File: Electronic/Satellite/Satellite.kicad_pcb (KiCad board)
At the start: 4 copper layers, 50 x 50 mm, 134 parts, among them CN1 SM04B-SRSS-TB, CN2 SM04B-SRSS-TB, J1 Conn02_Pin, J2 Conn02_Pin, J3 Conn02_Pin, J4 Conn02_Pin, J5 TC2050, J6 Conn_01x12_Pin, J7 Conn_01x12_Pin, SW1 TS-1088-AR02016, SW2 TS-1088-AR02016, U1 LAN8651B1-E/LMX, U10 SRR1280-560M, U11 NCP1117ST33T3G, U12 RP2354A, U13 WS2812C-2020-V6, U2 AVRH10C221KT1R5YA8, U3 MCP2518FDT-E/SL, U4 ATA6563-GAQW1, U5 AVRH10C221KT1R5YA8, U6 SY8513FCC, U7 MAX3232IPWR, U8 AL8860QMP-13, U9 ABM8-272-T3_C20625731, X1 ABM10-25.000MHZ-D30-T3

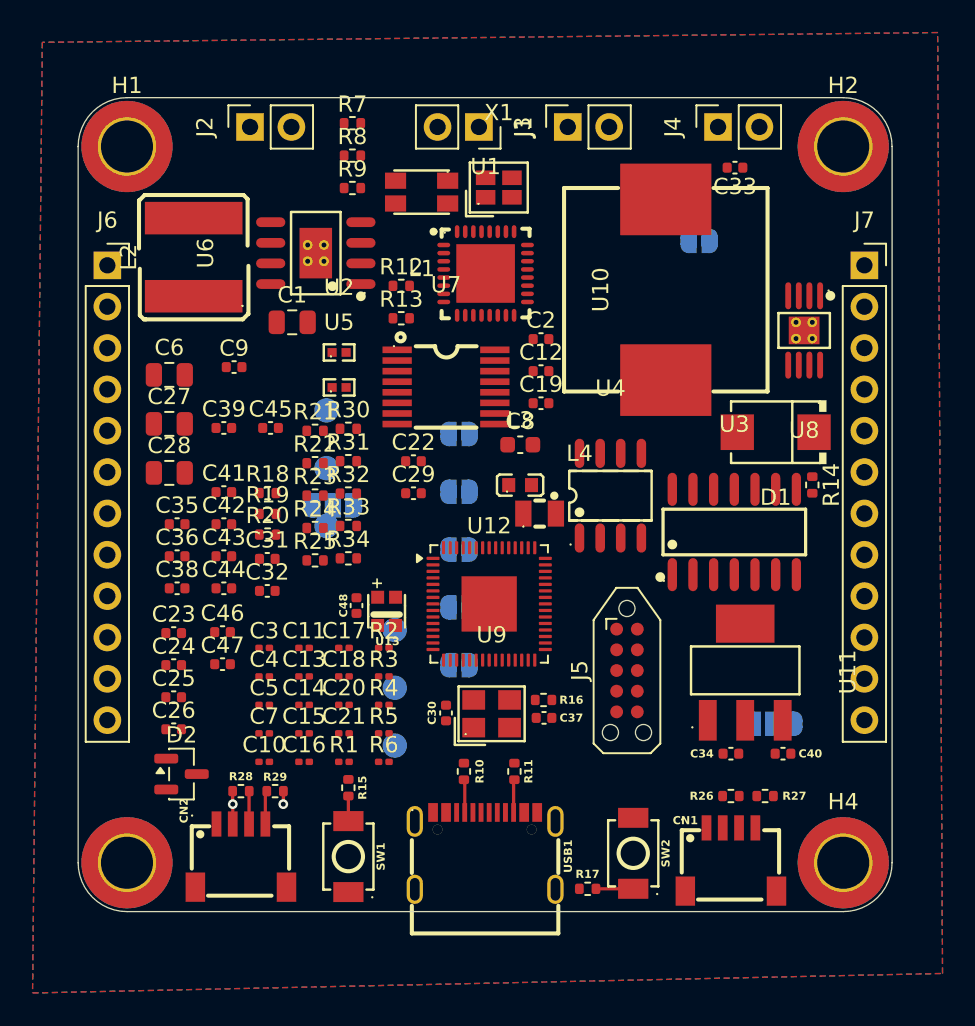
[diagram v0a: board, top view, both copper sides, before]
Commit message: WIP Satellite : reduce cob led current, layout + routing progress
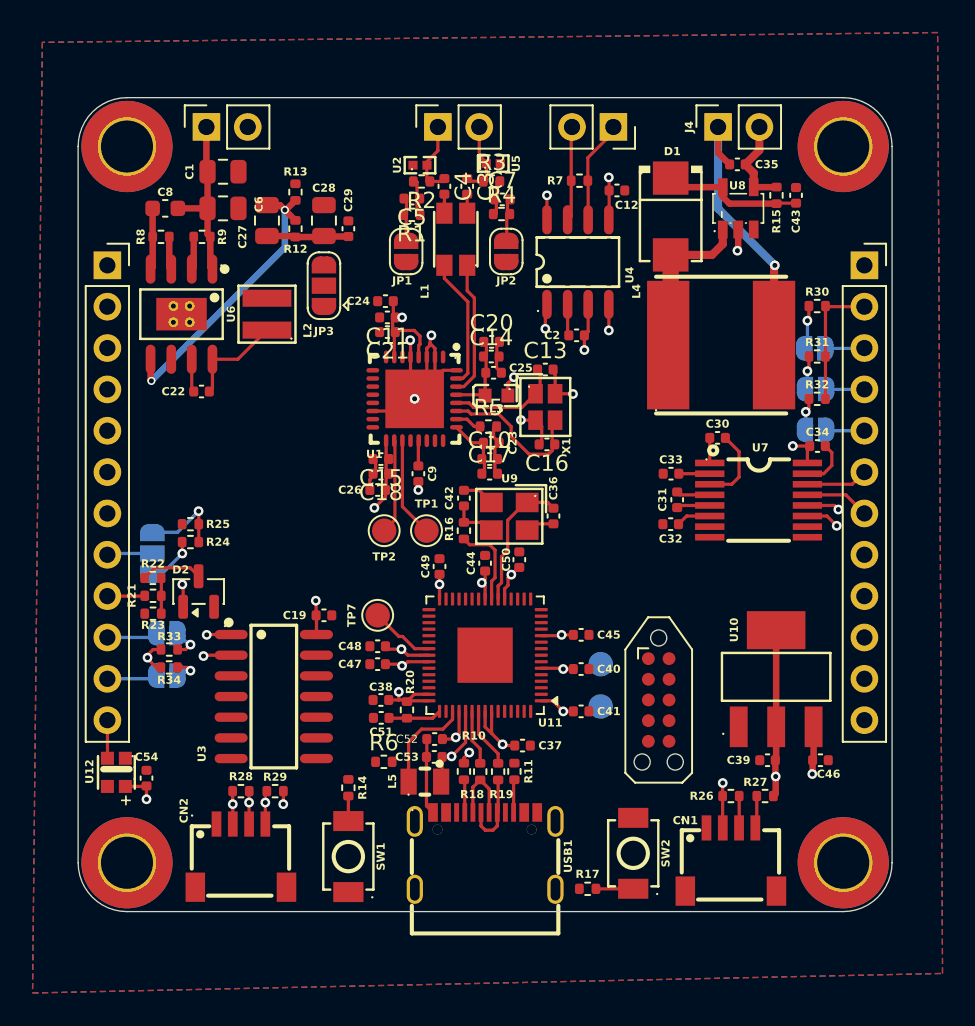
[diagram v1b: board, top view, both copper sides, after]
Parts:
- removed TP3, TP4: TestPoint, TestPoint:TestPoint_Pad_D1.5mm
- removed the U10 at (152.5, 93.0)
- added C30: 0.1uF, Capacitor_SMD:C_0402_1005Metric, F.Cu at (155.7, 102.1)
- added C31: 0.1uF, Capacitor_SMD:C_0402_1005Metric, F.Cu at (153.2, 105.9)
- added C32: 0.1uF, Capacitor_SMD:C_0402_1005Metric, F.Cu at (152.8, 107.4)
- added C33: 0.1uF, Capacitor_SMD:C_0402_1005Metric, F.Cu at (152.8, 104.3)
- added C34: 0.1uF, Capacitor_SMD:C_0402_1005Metric, F.Cu at (161.8, 102.6)
- added C43: 1uF, Capacitor_SMD:C_0402_1005Metric, F.Cu at (160.5, 87.2)
- added L4: ABG08A40M560, lcsc:IND-SMD_L8.0-W8.0_ABG08A40, F.Cu at (155.9, 96.4)
- C10, C11, C13, C14, C15, C16, C17, C18, C20, C21, C3, C4, C5, C7: footprint Capacitor_SMD:C_0201_0603Metric -> Capacitor_SMD:C_0402_1005Metric
- JP1, JP2, JP3, TP1, TP2, TP7: moved to F.Cu
- L2: value NR6045T100M -> APH303020C100MP03; footprint lcsc:IND-SMD_L6.0-W6.0_NR6045 -> lcsc:IND-SMD_L3.0-W3.0_FTC303012D
- R1, R2, R3, R4, R5, R6: footprint Resistor_SMD:R_0201_0603Metric -> Resistor_SMD:R_0402_1005Metric
- U8: value AL8860QMP-13 -> AL8860WT-7; footprint lcsc:MSOP-8_L3.0-W3.0-P0.65-LS4.9-BL-EP -> lcsc:SOT-23-5_L3.0-W1.7-P0.95-LS2.8-BR
- moved JP3 38.5 mm to (131.5, 92.8), turned to 90 degrees
- moved C7 35.9 mm to (142.5, 87.4)
- moved R1 33.9 mm to (136.9, 88.4), turned to 180 degrees
- moved C5 32.4 mm to (136.9, 87.4), turned to 180 degrees
- moved C4 32.1 mm to (138.9, 86.6), turned to -90 degrees
- moved R3 31.1 mm to (141.8, 86.3)
- moved R4 31.0 mm to (142.4, 88.3)
- moved C3 31.0 mm to (140.3, 86.6), turned to -90 degrees
- moved U3 30.0 mm to (128.4, 118.0), turned to -90 degrees
- moved R30 29.8 mm to (161.8, 94.0)
- moved R31 29.5 mm to (161.8, 97.1)
- moved R32 29.4 mm to (161.8, 99.7)
- moved R2 28.7 mm to (137.5, 86.3), turned to 180 degrees
- moved C25 28.0 mm to (141.9, 98.1)
- moved C41 26.6 mm to (147.3, 118.9)
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- renumbered C33 to C35, C30 to C36, C31 to C37, C32 to C38, C34 to C39, C35 to C40, C36 to C41, C37 to C42, C38 to C44, C39 to C45, C40 to C46, C41 to C47, C42 to C48, C43 to C49, C44 to C50, C45 to C51, C46 to C52, C47 to C53, C48 to C54, L4 to L5, R15 to R14, R14 to R15, U11 to U10, U12 to U11, U13 to U12
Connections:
- C12 pad 1: +3.3V -> +3V3
- C19 pad 1: +3.3V -> +3V3
- C27 pad 1: +5V -> Net-(JP3-B)
- C28 pad 1: +5V -> Net-(JP3-B)
- C29 pad 1: +5V -> Net-(JP3-B)
- C3 pad 1: Net-(C3-Pad1) -> Net-(J1-Pin_2)
- C4 pad 1: Net-(C4-Pad1) -> Net-(J1-Pin_1)
- C46 pad 1: /5V -> +5V
- J1 pad 1: /TRX_P -> Net-(J1-Pin_1)
- J1 pad 2: /TRX_N -> Net-(J1-Pin_2)
- JP3 pad 2: /5V -> +5V
- JP3 pad 3: +5V -> Net-(JP3-B)
- L2 pad 2: +5V -> Net-(JP3-B)
- R12 pad 1: +5V -> Net-(JP3-B)
- R2 pad 1: Net-(C4-Pad1) -> Net-(J1-Pin_1)
- R3 pad 1: Net-(C3-Pad1) -> Net-(J1-Pin_2)
- U1 pad 10: /MISO -> /SPI1_RX
- U1 pad 12: /CLK -> /SPI1_SCK
- U1 pad 13: /MOSI -> /SPI1_TX
- U10 pad 3: /5V -> +5V
- U11 pad 12: unconnected-(U12-GPIO8-Pad12) -> /LAN_RESET_N
- U11 pad 13: unconnected-(U12-GPIO9-Pad13) -> /IRQ_N
- U11 pad 17: unconnected-(U12-GPIO13-Pad17) -> /LAN_CS
- U11 pad 19: unconnected-(U12-GPIO15-Pad19) -> /CAN_INT
- U11 pad 34: unconnected-(U12-GPIO22-Pad34) -> /CAN_INT0
- U11 pad 35: unconnected-(U12-GPIO23-Pad35) -> /CAN_INT1
- U11 pad 36: unconnected-(U12-GPIO24-Pad36) -> /CAN_CS
- U2 pad 2: Net-(C4-Pad1) -> Net-(J1-Pin_1)
- U3 pad 14: +3.3V -> +3V3
- U4 pad 5: +3.3V -> +3V3
- U5 pad 1: Net-(C3-Pad1) -> Net-(J1-Pin_2)
- U7 pad 1: unconnected-(U7-C1+-Pad1) -> Net-(U7-C1+)
- U7 pad 15: unconnected-(U7-GND-Pad15) -> GND
- U7 pad 16: unconnected-(U7-VCC-Pad16) -> +3V3
- U7 pad 2: unconnected-(U7-V+-Pad2) -> Net-(U7-V+)
- U7 pad 3: unconnected-(U7-C1--Pad3) -> Net-(U7-C1-)
- U7 pad 4: unconnected-(U7-C2+-Pad4) -> Net-(U7-C2+)
- U7 pad 5: unconnected-(U7-C2--Pad5) -> Net-(U7-C2-)
- U7 pad 6: unconnected-(U7-V--Pad6) -> Net-(U7-V-)
- U8 pad 1: /COB_SET -> Net-(D1-A)
- U8 pad 3: GND -> /PWM_COB
- U8 pad 4: /PWM_COB -> /COB_SET
- U8 pad 5: Net-(D1-A) -> VCC
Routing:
- net +3V3: track 2.83 -> 71.0 mm, vias 2 -> 20
- net GND: track 0.00 -> 55.9 mm, vias 0 -> 10
- net Net-(U3-RXCAN): track 0.00 -> 40.1 mm, vias 0 -> 2
- net Net-(U3-TXCAN): track 0.00 -> 35.4 mm, vias 0 -> 2
- net Net-(U6-FB): track 0.00 -> 18.3 mm, vias 0 -> 2
- net Net-(J4-Pin_1): track 0.00 -> 17.5 mm, vias 0 -> 1
- net +1V1: track 0.00 -> 11.9 mm, vias 0 -> 4
- net Net-(J2-Pin_1): track 0.00 -> 10.7 mm
- net Net-(D1-A): track 0.00 -> 9.98 mm
- net /XTI: track 0.00 -> 9.36 mm
- net Net-(U1-VDDA): track 0.00 -> 9.09 mm
- net VCC: track 0.00 -> 8.71 mm
- net /XIN: track 0.00 -> 8.49 mm
- net /TRX_P: track 0.00 -> 8.35 mm
- net /TRX_N: track 0.00 -> 8.06 mm
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- added copper zone on In2.Cu, net +3V3
- removed copper zone on In2.Cu, net GND

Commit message: WIP Satellite : split into multiple board for ease of debug / simplification
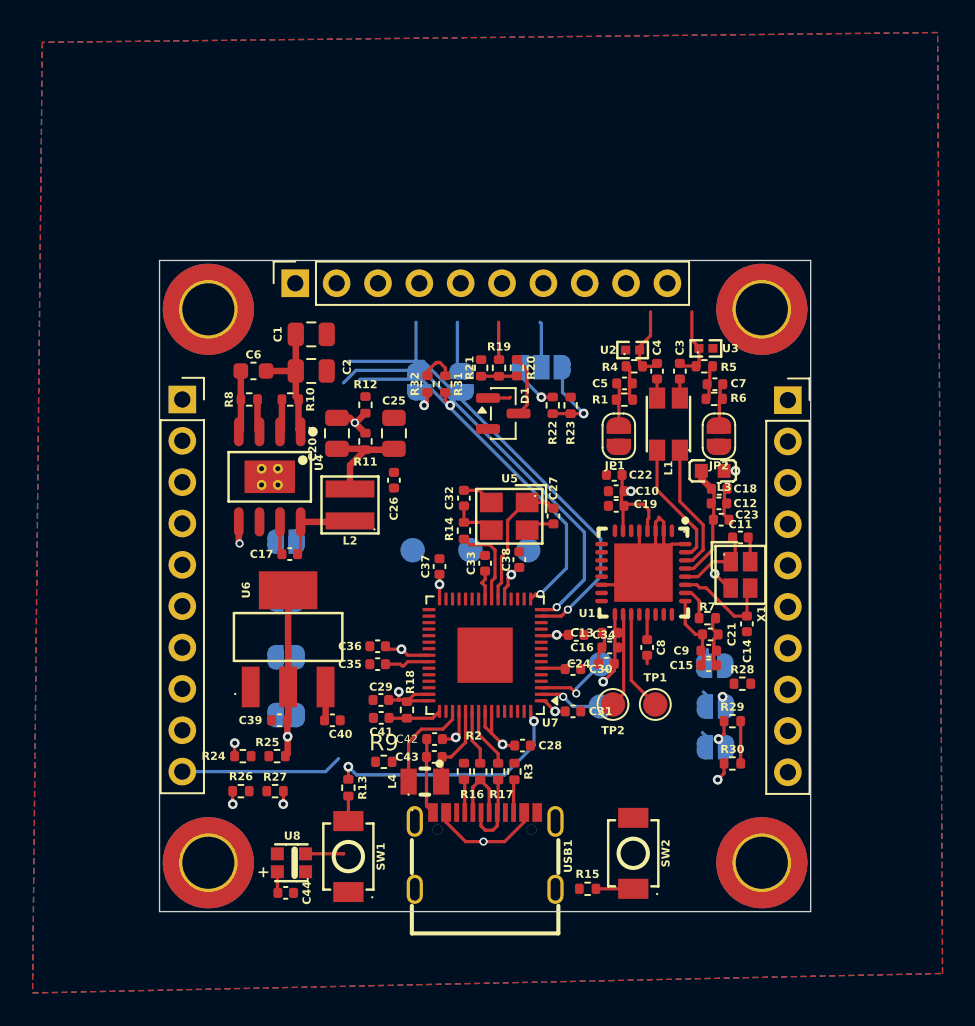
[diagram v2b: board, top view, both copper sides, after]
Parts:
- removed the C12 at (149.5, 86.9)
- removed the C19 at (131.5, 113.0)
- removed the C2 at (147.0, 95.8)
- removed the C30 at (155.7, 102.1)
- removed the C31 at (153.2, 105.9)
- removed the C32 at (152.8, 107.4)
- removed the C33 at (152.8, 104.3)
- removed the C34 at (161.8, 102.6)
- removed the C35 at (156.9, 85.3)
- removed the C43 at (160.5, 87.2)
- removed CN1, CN2: SM04B-SRSS-TB, lcsc:CONN-SMD_4P-P1.00_SM04B-SRSS-TB-LF-SN
- removed the D1 at (152.8, 88.5)
- removed J1, J2: Conn02_Pin, Connector_PinSocket_2.54mm:PinSocket_1x02_P2.54mm_Vertical
- removed J6, J7: Conn_01x12_Pin, Connector_PinSocket_2.54mm:PinSocket_1x12_P2.54mm_Vertical
- removed JP3: Jumper_3_Open, Jumper:SolderJumper-3_P1.3mm_Open_RoundedPad1.0x1.5mm
- removed the L4 at (155.9, 96.4)
- removed the R15 at (159.3, 87.2)
- removed the R7 at (147.2, 86.3)
- removed the TP7 at (134.8, 113.0)
- removed the U3 at (128.4, 118.0)
- removed the U4 at (147.1, 91.3)
- removed the U7 at (158.2, 105.9)
- removed the U8 at (156.9, 88.0)
- added JP5: JO, Jumper:SolderJumper-2_P1.3mm_Open_RoundedPad1.0x1.5mm, B.Cu at (129.2, 108.5)
- added JP6: JO, Jumper:SolderJumper-2_P1.3mm_Open_RoundedPad1.0x1.5mm, B.Cu at (129.2, 112.0)
- added JP7: JO, Jumper:SolderJumper-2_P1.3mm_Open_RoundedPad1.0x1.5mm, B.Cu at (129.2, 115.6)
- added JP8: JO, Jumper:SolderJumper-2_P1.3mm_Open_RoundedPad1.0x1.5mm, B.Cu at (129.2, 119.1)
- added TP3: TP, TestPoint:TestPoint_Pad_D1.5mm, B.Cu at (136.9, 109.0)
- added TP4: TP, TestPoint:TestPoint_Pad_D1.5mm, B.Cu at (140.5, 109.0)
- added TP5: TP, TestPoint:TestPoint_Pad_D1.5mm, B.Cu at (144.1, 109.0)
- J3, J4: value Conn02_Pin -> Conn_01x10; footprint Connector_PinSocket_2.54mm:PinSocket_1x02_P2.54mm_Vertical -> Connector_PinSocket_2.54mm:PinSocket_1x10_P2.54mm_Vertical
- J5: value TC2050 -> Conn_01x10; footprint Connector:Tag-Connect_TC2050-IDC-NL_2x05_P1.27mm_Vertical -> Connector_PinSocket_2.54mm:PinSocket_1x10_P2.54mm_Vertical
- moved J4 36.9 mm to (122.8, 99.7), turned to 0 degrees
- moved R24 30.1 mm to (126.5, 121.7)
- moved C39 30.1 mm to (128.8, 119.5)
- moved C40 30.1 mm to (132.0, 119.5)
- moved R25 30.1 mm to (128.6, 121.7)
- moved U6 30.1 mm to (129.3, 114.4)
- moved JP4 26.5 mm to (144.9, 97.8), turned to 180 degrees
- moved R20 25.8 mm to (143.4, 97.8), turned to -90 degrees
- moved R19 25.5 mm to (142.3, 97.8), turned to 90 degrees
- moved R21 25.2 mm to (141.2, 97.8), turned to -90 degrees
- moved R23 24.5 mm to (146.7, 100.1), turned to -90 degrees
- moved JP12 23.8 mm to (140.0, 98.7), turned to -90 degrees
- moved JP13 23.8 mm to (137.4, 98.7), turned to -90 degrees
- moved R22 23.8 mm to (145.6, 100.1), turned to -90 degrees
- moved R28 23.7 mm to (157.2, 117.2)
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- renumbered C11 to C10, C13 to C11, C14 to C12, C15 to C13, C16 to C14, C17 to C15, C18 to C16, C22 to C17, C20 to C18, C21 to C19, C6 to C2, C27 to C20, C23 to C21, C24 to C22, C25 to C23, C26 to C24, C28 to C25, C29 to C26, C36 to C27, C37 to C28, C38 to C29, C40 to C30, C41 to C31, C42 to C32, C44 to C33, C45 to C34, C47 to C35, C48 to C36, C49 to C37, C50 to C38, C46 to C40, C51 to C41, C52 to C42, C53 to C43, C54 to C44, C8 to C6, C9 to C8, C10 to C9, D2 to D1, JP6 to JP10, JP7 to JP11, JP8 to JP12, JP9 to JP13, JP5 to JP9, L5 to L4, R9 to R10, R12 to R11, R13 to R12, R14 to R13, R16 to R14, R17 to R15, R18 to R16, R19 to R17, R20 to R18, R21 to R19, R10 to R2, R22 to R20, R23 to R21, R24 to R22, R25 to R23, R26 to R24, R27 to R25, R28 to R26, R29 to R27, R30 to R28, R31 to R29, R11 to R3, R32 to R30, R33 to R31, R34 to R32, R2 to R4, R3 to R5, R4 to R6, R5 to R7, R6 to R9, TP5 to TP6, TP6 to TP7, U5 to U3, U6 to U4, U9 to U5, U10 to U6, U11 to U7, U12 to U8
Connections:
- net Net-(J1-Pin_1) renamed /SPE_N
- net Net-(J1-Pin_2) renamed /SPE_P
- C1 pad 1: Net-(J2-Pin_1) -> +12V
- C2 pad 1: Net-(J2-Pin_1) -> +12V
- C20 pad 1: Net-(JP3-B) -> +5V
- C25 pad 1: Net-(JP3-B) -> +5V
- C26 pad 1: Net-(JP3-B) -> +5V
- C6 pad 1: Net-(J2-Pin_1) -> +12V
- J3 pad 1: /CAN_L -> +12V
- J3 pad 2: /CAN_H -> /5V
- J4 pad 1: Net-(J4-Pin_1) -> /I2C0_SDA
- J4 pad 2: /COB_SET -> /I2C0_SCL
- J5 pad 1: +3V3 -> /GPIO6
- J5 pad 10: /SWDIO -> GND
- J5 pad 2: GND -> /GPIO7
- J5 pad 3: GND -> /GPIO8
- J5 pad 4: unconnected-(J5-Pad4) -> /RS232_TX
- J5 pad 5: unconnected-(J5-Pad5) -> /RS232_TX
- J5 pad 6: /RUN -> /SPI0_RX
- J5 pad 7: unconnected-(J5-Pad7) -> /GPIO17
- J5 pad 8: unconnected-(J5-Pad8) -> /SPI0_SCK
- J5 pad 9: /SWCLK -> /SPI0_TX
- JP4 pad 2: Net-(J6-Pin_8) -> Net-(J4-Pin_8)
- L2 pad 2: Net-(JP3-B) -> +5V
- R10 pad 2: Net-(J2-Pin_1) -> +12V
- R11 pad 1: Net-(JP3-B) -> +5V
- R19 pad 2: Net-(J6-Pin_9) -> Net-(J4-Pin_9)
- R24 pad 1: /I2C0_SDA -> Net-(JP5-B)
- R25 pad 1: /I2C0_SCL -> Net-(JP6-B)
- R26 pad 1: /I2C1_SDA -> Net-(JP7-B)
- R27 pad 1: /I2C1_SCL -> Net-(JP8-B)
- U4 pad 1: Net-(J2-Pin_1) -> +12V
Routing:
- net VBUS: track 0.00 -> 42.1 mm, vias 0 -> 1
- net Net-(U3-RXCAN): track 40.1 -> 0.00 mm, vias 2 -> 0
- net Net-(U3-TXCAN): track 35.4 -> 0.00 mm, vias 2 -> 0
- net /SPI1_SCK: track 0.00 -> 27.0 mm, vias 0 -> 1
- net /SPI1_TX: track 0.00 -> 25.6 mm, vias 0 -> 1
- net /SPI1_RX: track 0.00 -> 22.1 mm, vias 0 -> 1
- net +3V3: track 71.0 -> 53.1 mm, vias 20 -> 15
- net Net-(J4-Pin_1): track 17.5 -> 0.00 mm, vias 1 -> 0
- net /QSPI_SS: track 0.00 -> 15.3 mm, vias 0 -> 2
- net Net-(U4-FB): track 18.3 -> 4.38 mm
- net GND: track 55.9 -> 43.4 mm, vias 10 -> 1
- net Net-(J2-Pin_1): track 10.7 -> 0.00 mm
- net Net-(D1-A): track 9.98 -> 0.00 mm
- net /ADC2: track 3.11 -> 13.0 mm
- net VCC: track 8.71 -> 0.00 mm
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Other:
- board size 50 x 50 mm -> 40 x 40 mm

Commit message: Satellite PCB done !!!!!! (need verification)
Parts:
- removed JP4: Jumper_3_Open, Jumper:SolderJumper-3_P1.3mm_Open_RoundedPad1.0x1.5mm
- removed R22: 4.7K, Resistor_SMD:R_0402_1005Metric
- removed TP7: TP, TestPoint:TestPoint_Pad_D1.5mm
- R23: value 9.1K -> 10K
- moved JP8 30.1 mm to (157.3, 108.5)
- moved JP7 29.6 mm to (157.2, 105.9)
- moved R26 29.5 mm to (155.2, 117.5)
- moved R32 28.4 mm to (128.5, 125.6), turned to 0 degrees
- moved R27 27.2 mm to (155.2, 118.6), turned to 180 degrees
- moved R31 27.2 mm to (125.8, 122.5), turned to -90 degrees
- moved R24 26.9 mm to (134.1, 95.8), turned to 90 degrees
- moved R25 26.7 mm to (135.3, 95.8), turned to 90 degrees
- moved JP12 26.6 mm to (125.0, 120.7)
- moved JP13 26.6 mm to (127.4, 123.3)
- moved R23 26.5 mm to (125.1, 115.5), turned to 90 degrees
- moved JP11 25.6 mm to (152.7, 95.7), turned to -90 degrees
- moved R30 24.3 mm to (146.9, 99.8), turned to -90 degrees
- moved JP10 24.3 mm to (147.5, 95.7), turned to -90 degrees
- moved R29 23.2 mm to (144.3, 99.8), turned to -90 degrees
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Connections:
- J3 pad 10: GND -> /GPIO8
- J3 pad 2: /5V -> +5V
- J3 pad 4: unconnected-(J3-Pin_4-Pad4) -> /SPI0_TX
- J3 pad 5: unconnected-(J3-Pin_5-Pad5) -> /SPI0_SCK
- J3 pad 6: unconnected-(J3-Pin_6-Pad6) -> /GPIO17
- J3 pad 7: unconnected-(J3-Pin_7-Pad7) -> /SPI0_RX
- J3 pad 8: unconnected-(J3-Pin_8-Pad8) -> /GPIO7
- J3 pad 9: /ADC3 -> /GPIO6
- J4 pad 10: /ADC2 -> /ADC3
- J4 pad 3: /I2C1_SDA -> /GPIO22
- J4 pad 4: /I2C1_SCL -> /GPIO23
- J4 pad 5: /LED_Data_Out -> /GPIO24
- J4 pad 6: /UART1_TX -> /GPIO25
- J4 pad 7: /UART1_RX -> /ADC0
- J4 pad 9: Net-(J4-Pin_9) -> /ADC2
- J5 pad 1: /GPIO6 -> /UART1_RX
- J5 pad 2: /GPIO7 -> /UART1_TX
- J5 pad 3: /GPIO8 -> /I2C1_SDA
- J5 pad 4: /RS232_TX -> /I2C1_SCL
- J5 pad 5: /RS232_TX -> /UART0_RX
- J5 pad 6: /SPI0_RX -> /UART0_TX
- J5 pad 7: /GPIO17 -> /LED_Data_Out
- J5 pad 8: /SPI0_SCK -> GND
- J5 pad 9: /SPI0_TX -> GND
- R19 pad 2: Net-(J4-Pin_9) -> Net-(J4-Pin_8)
- TP6 pad 1: /UART0_TX -> VBUS
- U7 pad 34: /CAN_INT0 -> /GPIO22
- U7 pad 35: /CAN_INT1 -> /GPIO23
- U7 pad 36: /CAN_CS -> /GPIO24
- U7 pad 37: /PWM_COB -> /GPIO25
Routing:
- net GND: track 43.4 -> 85.9 mm, vias 1 -> 23
- net /LED_Data_Out: track 0.00 -> 35.3 mm, vias 0 -> 1
- net VBUS: track 42.1 -> 9.81 mm
- net +5V: track 8.47 -> 40.6 mm, vias 0 -> 2
- net /GPIO7: track 0.00 -> 30.2 mm
- net /RUN: track 0.00 -> 30.2 mm, vias 0 -> 2
- net /I2C0_SDA: track 0.00 -> 28.3 mm, vias 0 -> 1
- net /UART1_RX: track 0.00 -> 28.1 mm, vias 0 -> 1
- net /GPIO6: track 0.00 -> 27.6 mm, vias 0 -> 1
- net /LED_Data: track 0.00 -> 26.4 mm, vias 0 -> 2
- net /I2C1_SDA: track 0.00 -> 26.1 mm, vias 0 -> 1
- net /I2C0_SCL: track 0.00 -> 25.7 mm, vias 0 -> 1
- net /UART1_TX: track 0.00 -> 24.5 mm, vias 0 -> 1
- net /SPI0_RX: track 0.00 -> 22.0 mm
- net /I2C1_SCL: track 0.00 -> 21.9 mm, vias 0 -> 1
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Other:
- board text added: "ADC2 PULLUP"
- board text added: "ADC3 PULLUP"
- board text added: "BOOT"
- board text added: "I2C0 PULLUP"
- board text added: "I2C1 PULLUP"
- board text added: "PULLUP"
- board text added: "RESET"
- board text added: "RUN"
- board text added: "SPE Term"
- board text added: "SWCLK"
- board text added: "SWDIO"
- board text added: "Satellite V0.1"
- board text added: "VBUS"
